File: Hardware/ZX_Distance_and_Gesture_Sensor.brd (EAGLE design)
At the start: 55.9 x 12.7 mm, 47 parts, among them Q1 MMBT2222A, Q2 MOSFET-NCHANNEL2N7002PW, U1 BRM-2508VERT

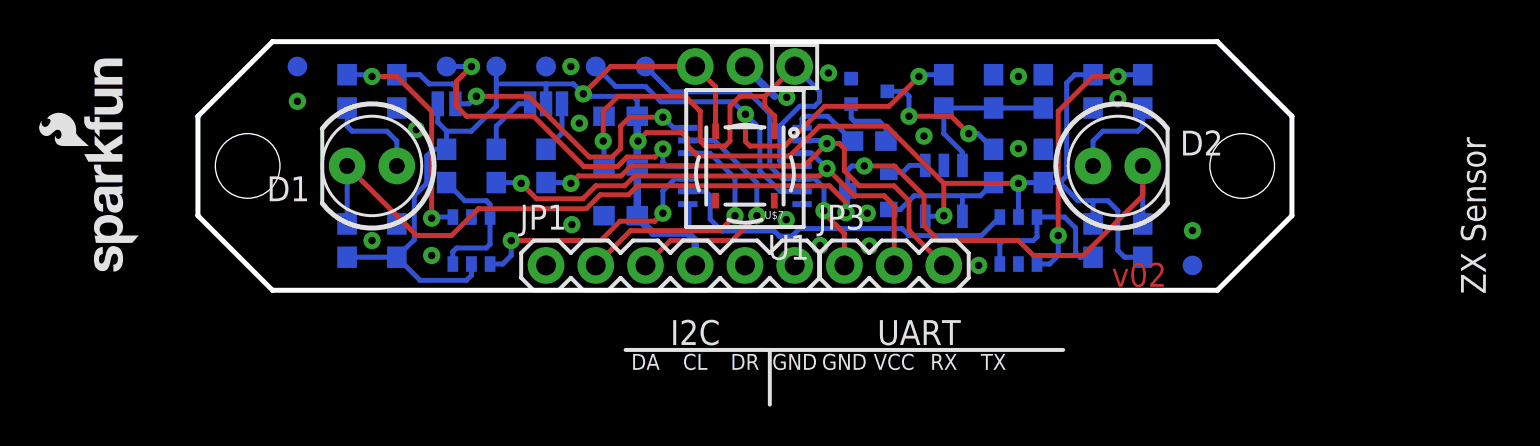
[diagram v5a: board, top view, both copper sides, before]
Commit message: Added silk pinout. Ready for v02 review.
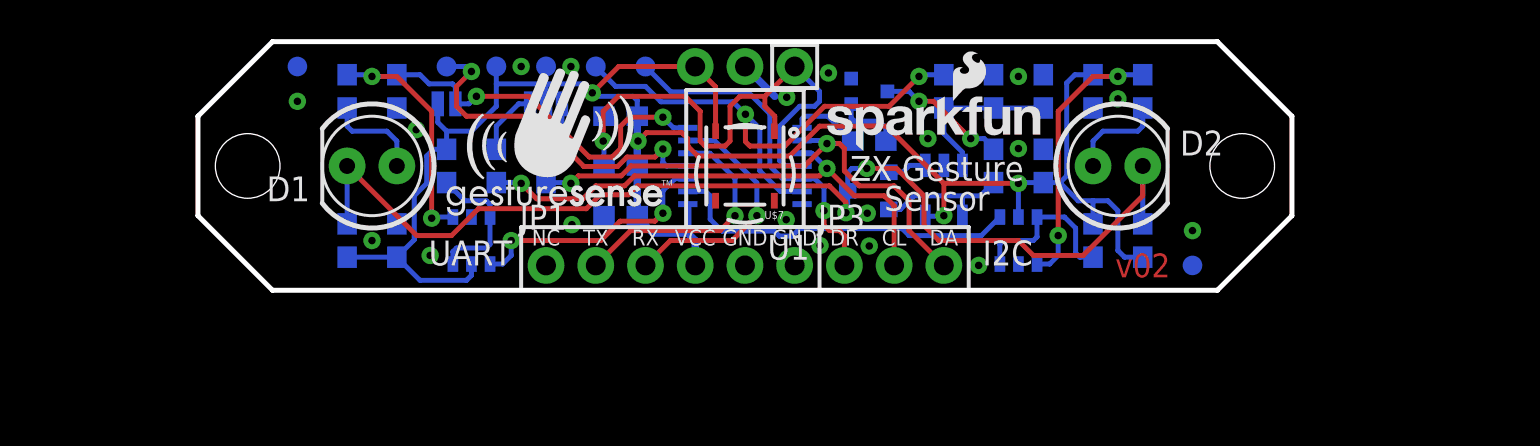
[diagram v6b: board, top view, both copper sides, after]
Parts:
- added U$6: GESTURESENSE_LOGOSTEXT, SparkFun-Aesthetics:GESTURESENSE_TEXT
- JP1: device SparkFun-Connectors:1X06 -> SparkFun-Connectors:1X06_NO_SILK
- JP3: device SparkFun-Connectors:1X03 -> SparkFun-Connectors:1X03_NO_SILK
- moved U$5 35.2 mm to (3.76, 0.66), turned to 0 degrees
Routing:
- net N$4: track 7.25 -> 6.69 mm
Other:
- board text added: "NC"
- board text added: "Sensor"
- board text added: "Shawn Hymel (SparkFun Electronics) with XYZ Interactive Technologies"
- board text added: "ZX Gesture"
- board text removed: "Shawn Hymel in collaboration with XYZ Interactive Technologies"
- board text removed: "ZX Sensor"

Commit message: Changed SMT receiver to DNP and removed DNP from PTH receiver and pullup resistor.
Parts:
- R9: value DNP -> 1K
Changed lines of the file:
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@@
 <setting verticaltext="up"/>
 </settings>
-<grid distance="0.05" unitdist="inch" unit="inch" style="dots" multiple="1" display="yes" altdistance="0.025" altunitdist="inch" altunit="inch"/>
+<grid distance="0.05" unitdist="inch" unit="inch" style="dots" multiple="1" display="yes" altdistance="0.005" altunitdist="inch" altunit="inch"/>
 <layers>
-<layer number="1" name="Top" color="4" fill="1" visible="yes" active="yes"/>
+<layer number="1" name="Top" color="4" fill="1" visible="no" active="yes"/>
 <layer number="2" name="Route2" color="1" fill="3" visible="no" active="yes"/>
 <layer number="15" name="Route15" color="4" fill="6" visible="no" active="yes"/>
@@
 <layer number="19" name="Unrouted" color="6" fill="1" visible="yes" active="yes"/>
 <layer number="20" name="Dimension" color="15" fill="1" visible="yes" active="yes"/>
-<layer number="21" name="tPlace" color="16" fill="1" visible="yes" active="yes"/>
+<layer number="21" name="tPlace" color="16" fill="1" visible="no" active="yes"/>
 <layer number="22" name="bPlace" color="14" fill="1" visible="yes" active="yes"/>
-<layer number="23" name="tOrigins" color="15" fill="1" visible="yes" active="yes"/>
+<layer number="23" name="tOrigins" color="15" fill="1" visible="no" active="yes"/>
 <layer number="24" name="bOrigins" color="15" fill="1" visible="yes" active="yes"/>
 <layer number="25" name="tNames" color="7" fill="1" visible="no" active="yes"/>
@@
 <layer number="43" name="vRestrict" color="2" fill="10" visible="no" active="yes"/>
 <layer number="44" name="Drills" color="7" fill="1" visible="no" active="yes"/>
-<layer number="45" name="Holes" color="7" fill="1" visible="yes" active="yes"/>
+<layer number="45" name="Holes" color="7" fill="1" visible="no" active="yes"/>
 <layer number="46" name="Milling" color="3" fill="1" visible="no" active="yes"/>
-<layer number="51" name="tDocu" color="6" fill="1" visible="yes" active="yes"/>
+<layer number="51" name="tDocu" color="6" fill="1" visible="no" active="yes"/>
 <layer number="52" name="bDocu" color="7" fill="1" visible="no" active="yes"/>
 <layer number="3" name="Route3" color="4" fill="3" visible="no" active="no"/>
@@
 <element name="U$7" library="SparkFun-Sensors" package="TSOP572" value="TSOP57238TT1" x="0" y="0" rot="R180">
 <attribute name="PROD_ID" value="COMP-11990" x="-15.24" y="33.02" size="1.778" layer="27" rot="R180" display="off"/>
+<attribute name="PLACE" value="DNP" x="0" y="0" size="1.778" layer="27" rot="R180" display="off"/>
 </element>
 <element name="JP1" library="SparkFun-Connectors" package="1X06_NO_SILK" value="" x="-10.16" y="-5.08"/>
@@
 <attribute name="PROD_ID" value="CAP-00867" x="64.77" y="-48.26" size="1.778" layer="28" rot="MR270" display="off"/>
 </element>
-<element name="R9" library="SparkFun-Resistors" package="0603-RES" value="DNP" x="-6.35" y="0" rot="MR180"/>
+<element name="R9" library="SparkFun-Resistors" package="0603-RES" value="1K" x="-6.35" y="0" rot="MR180">
+<attribute name="PROD_ID" value="RES-07856" x="-6.35" y="0" size="1.778" layer="28" rot="MR180" display="off"/>
+<attribute name="VALUE" value="1K" x="-6.35" y="0" size="1.778" layer="28" rot="MR180" display="off"/>
+</element>
 <element name="C7" library="SparkFun-Capacitors" package="0603-CAP" value="4.7uF" x="-6.35" y="2.54" rot="MR0">
 <attribute name="PROD_ID" value="CAP-08280" x="-54.61" y="-41.91" size="1.778" layer="28" rot="MR0" display="off"/>
@@
 <element name="U1" library="SparkFun-Sensors" package="BRM-2508_VERT" value="BRM-2508VERT" x="0" y="5.08" rot="R180">
 <attribute name="PROD_ID" value="COMP-12059" x="0" y="5.08" size="1.778" layer="27" font="vector" ratio="15" rot="R180" display="off"/>
-<attribute name="PLACE" value="DNP" x="0" y="5.08" size="1.778" layer="27" rot="R180" display="off"/>
 </element>
 <element name="U$6" library="SparkFun-Aesthetics" package="GESTURESENSE_TEXT" value="GESTURESENSE_LOGOSTEXT" x="-15.24" y="-2.54"/>

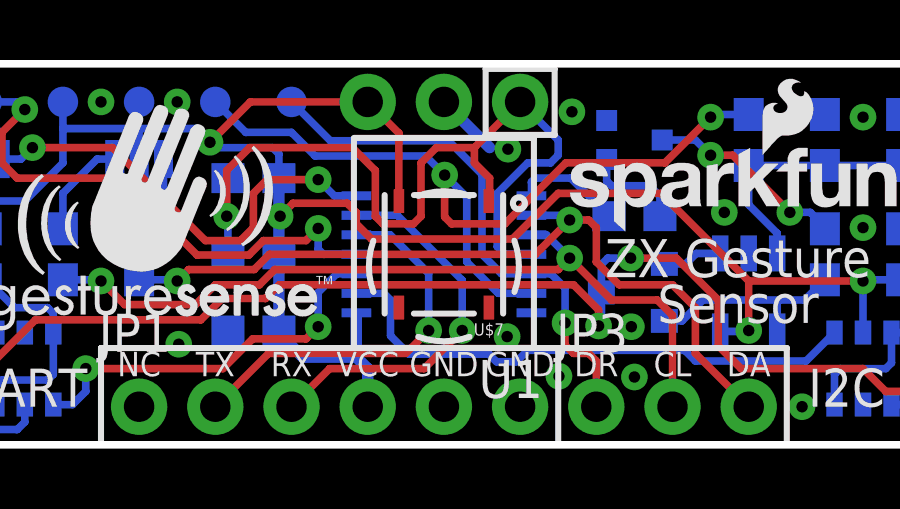
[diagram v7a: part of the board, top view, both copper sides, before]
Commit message: Swapped TX/RX. Added diagonal trace from GND header to pour.
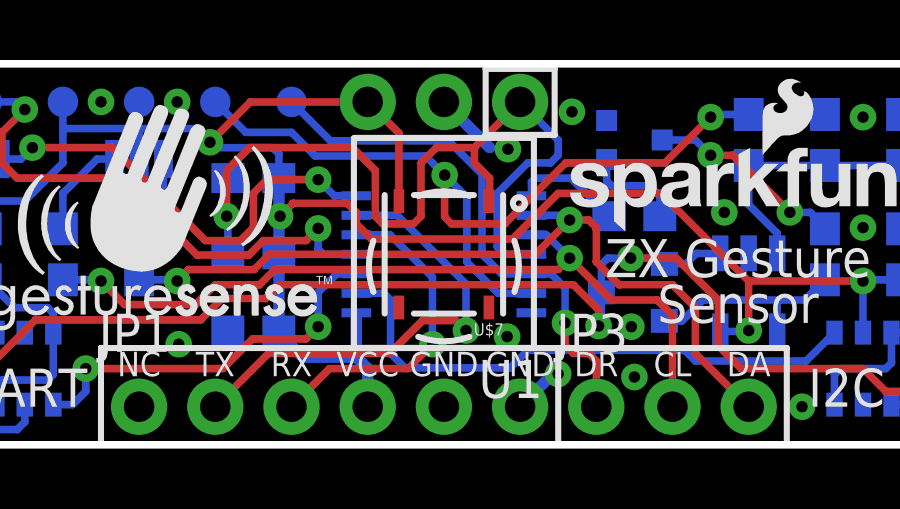
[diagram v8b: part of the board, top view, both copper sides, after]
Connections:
- net UART_RX: now also JP1.2; no longer JP1.3
- net UART_TX: now also JP1.3; no longer JP1.2
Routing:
- net UART_RX: track 12.8 -> 15.8 mm
- net UART_TX: track 13.0 -> 10.9 mm
- net GND: track 2.16 -> 3.98 mm
- net EM2: track 18.3 -> 18.8 mm
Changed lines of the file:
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@@
 <setting verticaltext="up"/>
 </settings>
-<grid distance="0.05" unitdist="inch" unit="inch" style="dots" multiple="1" display="yes" altdistance="0.005" altunitdist="inch" altunit="inch"/>
+<grid distance="0.001" unitdist="inch" unit="inch" style="dots" multiple="1" display="yes" altdistance="0.0001" altunitdist="inch" altunit="inch"/>
 <layers>
-<layer number="1" name="Top" color="4" fill="1" visible="no" active="yes"/>
+<layer number="1" name="Top" color="4" fill="1" visible="yes" active="yes"/>
 <layer number="2" name="Route2" color="1" fill="3" visible="no" active="yes"/>
 <layer number="15" name="Route15" color="4" fill="6" visible="no" active="yes"/>
@@
 <layer number="19" name="Unrouted" color="6" fill="1" visible="yes" active="yes"/>
 <layer number="20" name="Dimension" color="15" fill="1" visible="yes" active="yes"/>
-<layer number="21" name="tPlace" color="16" fill="1" visible="no" active="yes"/>
+<layer number="21" name="tPlace" color="16" fill="1" visible="yes" active="yes"/>
 <layer number="22" name="bPlace" color="14" fill="1" visible="yes" active="yes"/>
-<layer number="23" name="tOrigins" color="15" fill="1" visible="no" active="yes"/>
+<layer number="23" name="tOrigins" color="15" fill="1" visible="yes" active="yes"/>
 <layer number="24" name="bOrigins" color="15" fill="1" visible="yes" active="yes"/>
 <layer number="25" name="tNames" color="7" fill="1" visible="no" active="yes"/>
@@
 <layer number="43" name="vRestrict" color="2" fill="10" visible="no" active="yes"/>
 <layer number="44" name="Drills" color="7" fill="1" visible="no" active="yes"/>
-<layer number="45" name="Holes" color="7" fill="1" visible="no" active="yes"/>
+<layer number="45" name="Holes" color="7" fill="1" visible="yes" active="yes"/>
 <layer number="46" name="Milling" color="3" fill="1" visible="no" active="yes"/>
-<layer number="51" name="tDocu" color="6" fill="1" visible="no" active="yes"/>
+<layer number="51" name="tDocu" color="6" fill="1" visible="yes" active="yes"/>
 <layer number="52" name="bDocu" color="7" fill="1" visible="no" active="yes"/>
 <layer number="3" name="Route3" color="4" fill="3" visible="no" active="no"/>
@@
 <param name="dpGapFactor" value="2.5"/>
 <param name="checkGrid" value="0"/>
-<param name="checkAngle" value="0"/>
+<param name="checkAngle" value="1"/>
 <param name="checkFont" value="1"/>
 <param name="checkRestrict" value="1"/>
@@
 <signals>
 <signal name="UART_TX">
+<contactref element="U$1" pad="5"/>
+<via x="-0.381" y="-2.9972" extent="1-16" drill="0.381"/>
+<wire x1="-0.381" y1="-0.762" x2="-1.793" y2="0.65" width="0.254" layer="16"/>
+<wire x1="-2.9178" y1="0.65" x2="-1.793" y2="0.65" width="0.254" layer="16"/>
+<contactref element="JP1" pad="3"/>
+<wire x1="-5.08" y1="-5.08" x2="-3.81" y2="-3.81" width="0.254" layer="1"/>
+<wire x1="-3.81" y1="-3.81" x2="-1.1938" y2="-3.81" width="0.254" layer="1"/>
+<wire x1="-1.1938" y1="-3.81" x2="-0.381" y2="-2.9972" width="0.254" layer="1"/>
+<wire x1="-0.381" y1="-2.9972" x2="-0.381" y2="-0.762" width="0.254" layer="16"/>
+</signal>
+<signal name="UART_RX">
+<contactref element="U$1" pad="6"/>
+<via x="0.7366" y="-2.54" extent="1-16" drill="0.381"/>
+<wire x1="0.7366" y1="-0.9906" x2="-1.554" y2="1.3" width="0.254" layer="16"/>
+<wire x1="-2.9178" y1="1.3" x2="-1.554" y2="1.3" width="0.254" layer="16"/>
 <contactref element="JP1" pad="2"/>
-<contactref element="U$1" pad="5"/>
-<via x="-0.508" y="-2.54" extent="1-16" drill="0.381"/>
-<wire x1="-2.9178" y1="0.65" x2="-1.793" y2="0.65" width="0.254" layer="16"/>
 <wire x1="-7.62" y1="-5.08" x2="-5.842" y2="-3.302" width="0.254" layer="1"/>
-<wire x1="-5.842" y1="-3.302" x2="-1.27" y2="-3.302" width="0.254" layer="1"/>
-<wire x1="-1.27" y1="-3.302" x2="-0.508" y2="-2.54" width="0.254" layer="1"/>
-<wire x1="-0.508" y1="-2.54" x2="-0.508" y2="-0.635" width="0.254" layer="16"/>
-<wire x1="-0.508" y1="-0.635" x2="-1.793" y2="0.65" width="0.254" layer="16"/>
-</signal>
-<signal name="UART_RX">
-<contactref element="JP1" pad="3"/>
-<contactref element="U$1" pad="6"/>
-<via x="0.6096" y="-2.54" extent="1-16" drill="0.381"/>
-<wire x1="-2.9178" y1="1.3" x2="-1.554" y2="1.3" width="0.254" layer="16"/>
-<wire x1="-5.08" y1="-5.08" x2="-3.81" y2="-3.81" width="0.254" layer="1"/>
-<wire x1="0.6096" y1="-2.54" x2="0.6096" y2="-0.8636" width="0.254" layer="16"/>
-<wire x1="0.6096" y1="-0.8636" x2="-1.554" y2="1.3" width="0.254" layer="16"/>
-<wire x1="-3.81" y1="-3.81" x2="-0.6604" y2="-3.81" width="0.254" layer="1"/>
-<wire x1="-0.6604" y1="-3.81" x2="0.6096" y2="-2.54" width="0.254" layer="1"/>
+<wire x1="-5.842" y1="-3.302" x2="-1.8034" y2="-3.302" width="0.254" layer="1"/>
+<wire x1="-1.8034" y1="-3.302" x2="-0.7112" y2="-2.2098" width="0.254" layer="1"/>
+<wire x1="-0.7112" y1="-2.2098" x2="0.4064" y2="-2.2098" width="0.254" layer="1"/>
+<wire x1="0.4064" y1="-2.2098" x2="0.7366" y2="-2.54" width="0.254" layer="1"/>
+<wire x1="0.7366" y1="-0.9906" x2="0.7366" y2="-2.54" width="0.254" layer="16"/>
 </signal>
 <signal name="VCC">
@@
 <via x="11.938" y="-5.08" extent="1-16" drill="0.381"/>
 <via x="2.1082" y="-2.7432" extent="1-16" drill="0.381"/>
-<via x="3.8354" y="-4.064" extent="1-16" drill="0.381"/>
 <via x="-11.43" y="5.08" extent="1-16" drill="0.381"/>
 <via x="-16.0782" y="-4.572" extent="1-16" drill="0.381"/>
@@
 <via x="-8.8392" y="-2.9972" extent="1-16" drill="0.381"/>
 <via x="4.2672" y="4.7498" extent="1-16" drill="0.381"/>
+<wire x1="6.2484" y1="-2.413" x2="6.223" y2="-2.413" width="0.254" layer="16"/>
+<wire x1="3.81" y1="-3.81" x2="2.54" y2="-5.08" width="0.381" layer="16"/>
+<via x="3.81" y="-3.9878" extent="1-16" drill="0.381"/>
 </signal>
 <signal name="I2C_SDA">
@@
 <wire x1="12.074" y1="-3.556" x2="8.382" y2="-3.556" width="0.254" layer="16"/>
 <wire x1="8.382" y1="-3.556" x2="8.0264" y2="-3.2004" width="0.254" layer="16"/>
-<wire x1="-1.778" y1="-1.524" x2="-1.778" y2="-2.7178" width="0.254" layer="16"/>
-<wire x1="-1.778" y1="-2.7178" x2="-1.1684" y2="-3.3274" width="0.254" layer="16"/>
-<wire x1="2.794" y1="-3.2004" x2="2.413" y2="-3.5814" width="0.254" layer="16"/>
-<wire x1="-1.1684" y1="-3.3274" x2="1.4986" y2="-3.3274" width="0.254" layer="16"/>
-<wire x1="1.4986" y1="-3.3274" x2="1.7526" y2="-3.5814" width="0.254" layer="16"/>
-<wire x1="1.7526" y1="-3.5814" x2="2.413" y2="-3.5814" width="0.254" layer="16"/>
+<wire x1="-1.778" y1="-1.524" x2="-1.778" y2="-3.302" width="0.254" layer="16"/>
+<wire x1="2.794" y1="-3.2004" x2="2.2098" y2="-3.7846" width="0.254" layer="16"/>
 <wire x1="2.794" y1="-3.2004" x2="8.0264" y2="-3.2004" width="0.254" layer="16"/>
+<wire x1="-1.778" y1="-3.302" x2="-1.2954" y2="-3.7846" width="0.254" layer="16"/>
+<wire x1="-1.2954" y1="-3.7846" x2="2.2098" y2="-3.7846" width="0.254" layer="16"/>
 </signal>
 <signal name="N$9">
